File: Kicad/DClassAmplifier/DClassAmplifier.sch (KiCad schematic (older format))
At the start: 0 parts

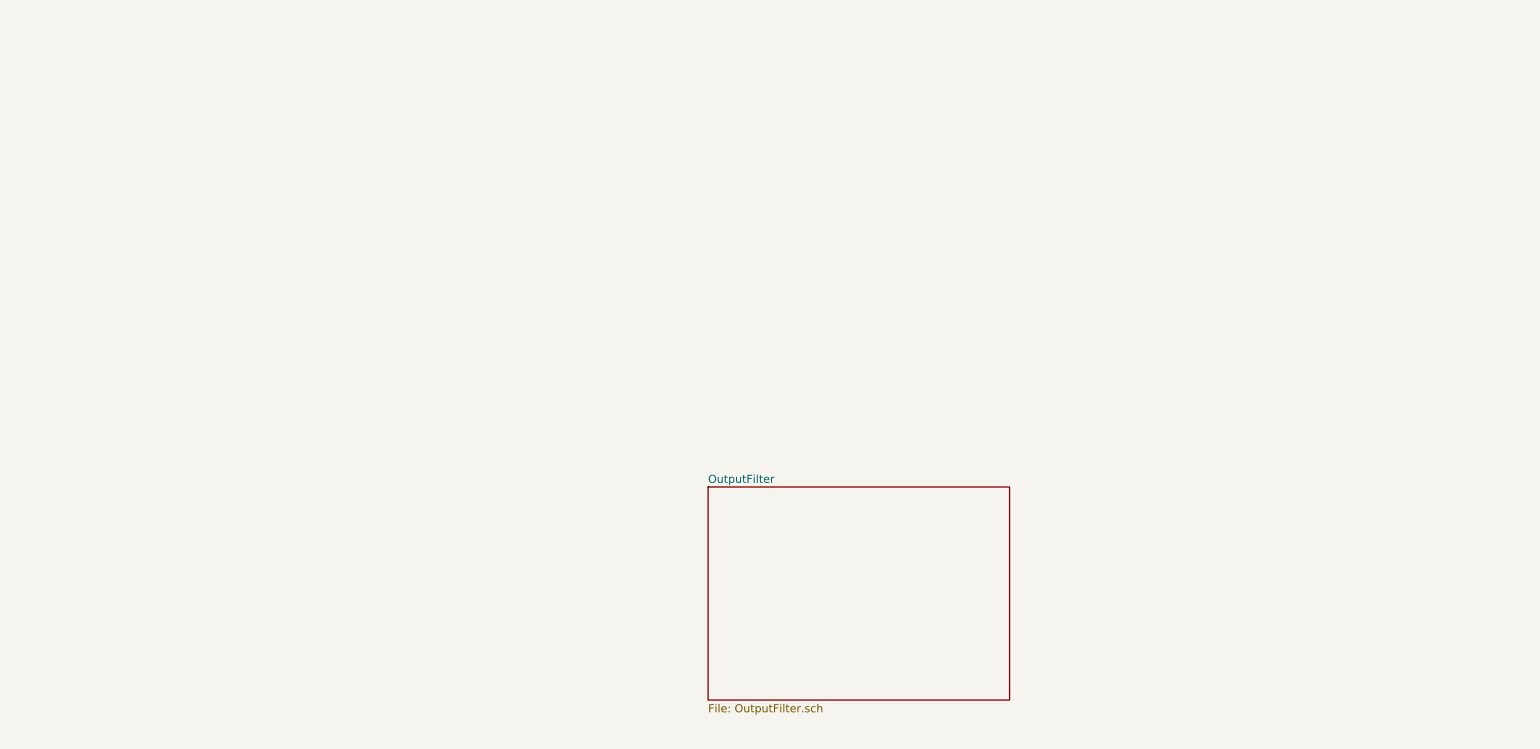
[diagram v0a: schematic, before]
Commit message: Added Net-Tied Grounds and Filter schematic
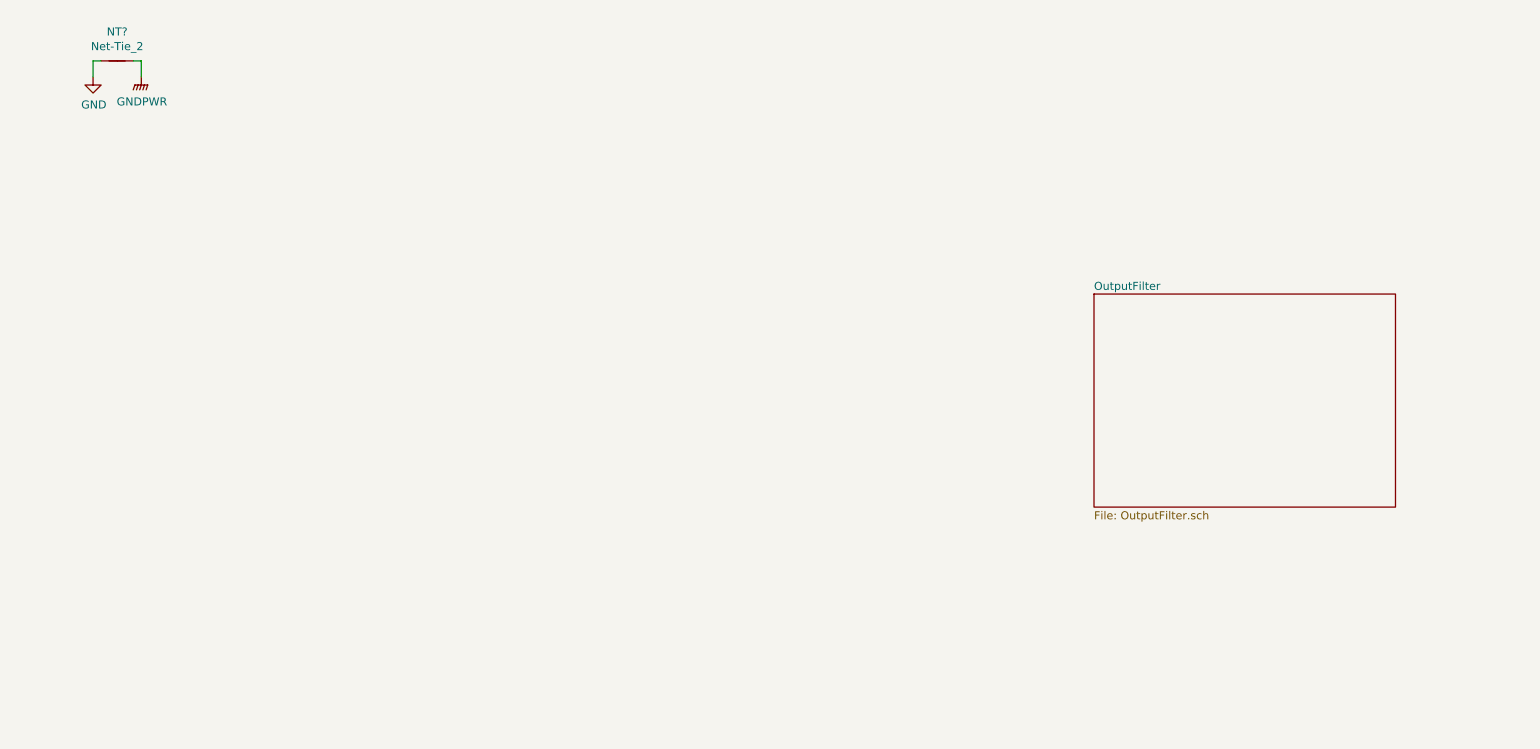
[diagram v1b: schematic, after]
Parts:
- added NT?: Net-Tie_2, NetTie:NetTie-2_SMD_Pad2.0mm, symbol Device:Net-Tie_2
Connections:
- new net GND: NT?.1
- new net GNDPWR: NT?.2
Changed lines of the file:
@@
 $EndDescr
 $Sheet
-S 4975 3550 1875 1325
+S 7375 2350 1875 1325
 U 60F78807
 F0 "OutputFilter" 50
 F1 "OutputFilter.sch" 50
 $EndSheet
+$Comp
+L power:GNDPWR #PWR?
+U 1 1 60FD17D7
+P 1450 1000
+F 0 "#PWR?" H 1450 800 50  0001 C CNN
+F 1 "GNDPWR" H 1454 846 50  0000 C CNN
+F 2 "" H 1450 950 50  0001 C CNN
+F 3 "" H 1450 950 50  0001 C CNN
+	1    1450 1000
+	1    0    0    -1
+$EndComp
+$Comp
+L power:GND #PWR?
+U 1 1 60FD1A94
+P 1150 1000
+F 0 "#PWR?" H 1150 750 50  0001 C CNN
+F 1 "GND" H 1155 827 50  0000 C CNN
+F 2 "" H 1150 1000 50  0001 C CNN
+F 3 "" H 1150 1000 50  0001 C CNN
+	1    1150 1000
+	1    0    0    -1
+$EndComp
+$Comp
+L Device:Net-Tie_2 NT?
+U 1 1 60FD21E0
+P 1300 900
+F 0 "NT?" H 1300 1081 50  0000 C CNN
+F 1 "Net-Tie_2" H 1300 990 50  0000 C CNN
+F 2 "NetTie:NetTie-2_SMD_Pad2.0mm" H 1300 900 50  0001 C CNN
+F 3 "~" H 1300 900 50  0001 C CNN
+	1    1300 900
+	1    0    0    -1
+$EndComp
+Wire Wire Line
+	1200 900  1150 900
+Wire Wire Line
+	1150 900  1150 1000
+Wire Wire Line
+	1400 900  1450 900
+Wire Wire Line
+	1450 900  1450 1000
 $EndSCHEMATC

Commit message: Create Additional Needed Hierarchical Schematics. Add Mounting Holes
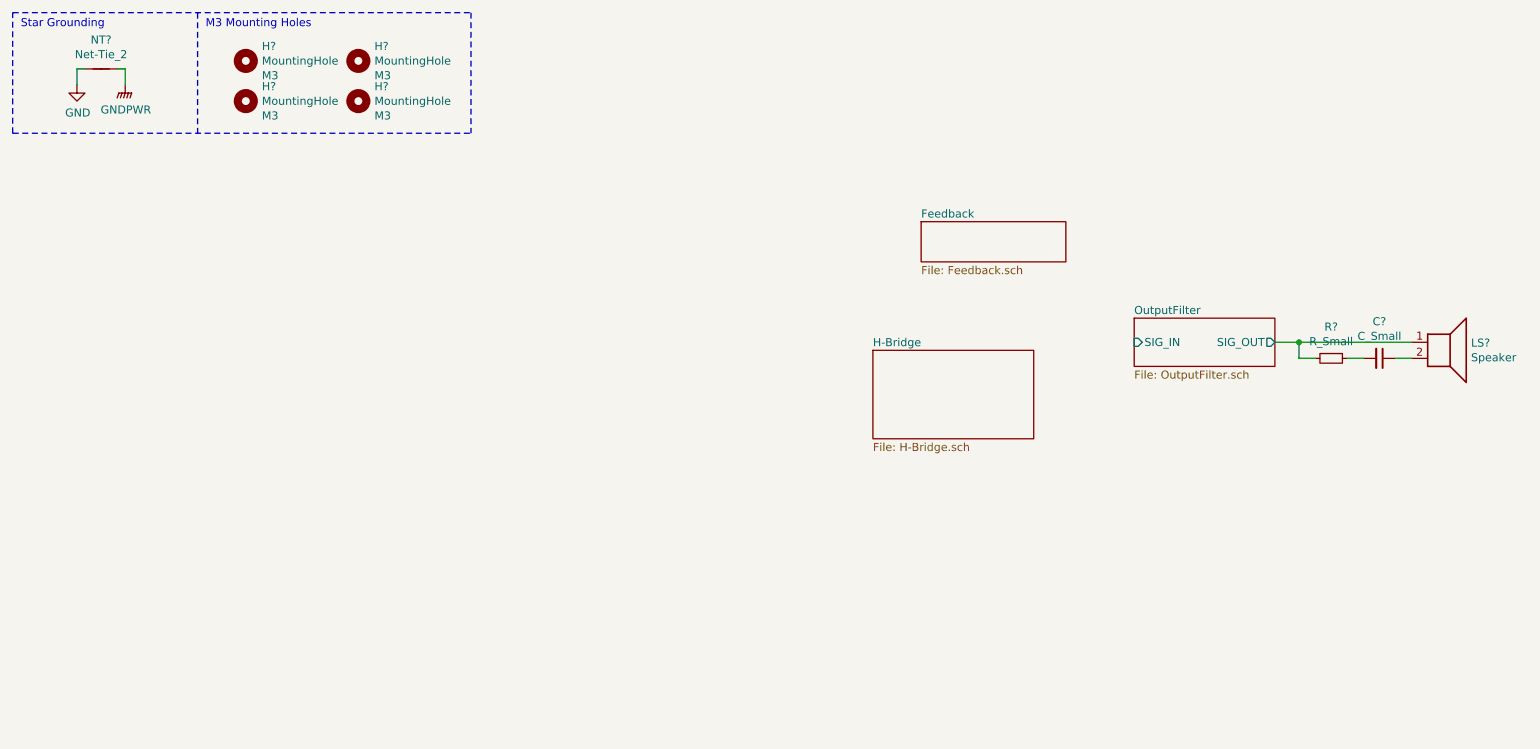
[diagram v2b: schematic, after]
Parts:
- added C?: C_Small, symbol Device:C_Small
- added H? (x4): MountingHole, MountingHole:MountingHole_3.2mm_M3_ISO7380_Pad, symbol Mechanical:MountingHole
- added LS?: Speaker, symbol Device:Speaker
- added R?: R_Small, symbol Device:R_Small
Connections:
- new net: C?.1, LS?.2
- new net: C?.2, R?.1
- new net OutputFilter/SIG_OUT: LS?.1, R?.2
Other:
- note added: "M3 Mounting Holes"
- note added: "Star Grounding"
- moved on the sheet: NT?
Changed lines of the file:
@@
 $Descr A4 11693 8268
 encoding utf-8
-Sheet 1 2
+Sheet 1 3
 Title ""
 Date ""
@@
 $EndDescr
 $Sheet
-S 7375 2350 1875 1325
+S 7625 2500 875  300
 U 60F78807
 F0 "OutputFilter" 50
 F1 "OutputFilter.sch" 50
+F2 "SIG_IN" I L 7625 2650 50
+F3 "SIG_OUT" O R 8500 2650 50
 $EndSheet
 $Comp
 L power:GNDPWR #PWR?
 U 1 1 60FD17D7
-P 1450 1000
-F 0 "#PWR?" H 1450 800 50  0001 C CNN
-F 1 "GNDPWR" H 1454 846 50  0000 C CNN
-F 2 "" H 1450 950 50  0001 C CNN
-F 3 "" H 1450 950 50  0001 C CNN
-	1    1450 1000
+P 1350 1050
+F 0 "#PWR?" H 1350 850 50  0001 C CNN
+F 1 "GNDPWR" H 1354 896 50  0000 C CNN
+F 2 "" H 1350 1000 50  0001 C CNN
+F 3 "" H 1350 1000 50  0001 C CNN
+	1    1350 1050
 	1    0    0    -1
 $EndComp
@@
 L power:GND #PWR?
 U 1 1 60FD1A94
-P 1150 1000
-F 0 "#PWR?" H 1150 750 50  0001 C CNN
-F 1 "GND" H 1155 827 50  0000 C CNN
-F 2 "" H 1150 1000 50  0001 C CNN
-F 3 "" H 1150 1000 50  0001 C CNN
-	1    1150 1000
+P 1050 1050
+F 0 "#PWR?" H 1050 800 50  0001 C CNN
+F 1 "GND" H 1055 877 50  0000 C CNN
+F 2 "" H 1050 1050 50  0001 C CNN
+F 3 "" H 1050 1050 50  0001 C CNN
+	1    1050 1050
 	1    0    0    -1
 $EndComp
@@
 L Device:Net-Tie_2 NT?
 U 1 1 60FD21E0
-P 1300 900
-F 0 "NT?" H 1300 1081 50  0000 C CNN
-F 1 "Net-Tie_2" H 1300 990 50  0000 C CNN
-F 2 "NetTie:NetTie-2_SMD_Pad2.0mm" H 1300 900 50  0001 C CNN
-F 3 "~" H 1300 900 50  0001 C CNN
-	1    1300 900
+P 1200 950
+F 0 "NT?" H 1200 1131 50  0000 C CNN
+F 1 "Net-Tie_2" H 1200 1040 50  0000 C CNN
+F 2 "NetTie:NetTie-2_SMD_Pad2.0mm" H 1200 950 50  0001 C CNN
+F 3 "~" H 1200 950 50  0001 C CNN
+	1    1200 950
 	1    0    0    -1
 $EndComp
 Wire Wire Line
-	1200 900  1150 900
+	1100 950  1050 950
 Wire Wire Line
-	1150 900  1150 1000
+	1050 950  1050 1050
 Wire Wire Line
-	1400 900  1450 900
+	1300 950  1350 950
 Wire Wire Line
-	1450 900  1450 1000
+	1350 950  1350 1050
+$Comp
+L Device:Speaker LS?
+U 1 1 60FD7EA0
+P 9550 2650
+F 0 "LS?" H 9720 2646 50  0000 L CNN
+F 1 "Speaker" H 9720 2555 50  0000 L CNN
+F 2 "" H 9550 2450 50  0001 C CNN
+F 3 "~" H 9540 2600 50  0001 C CNN
+	1    9550 2650
+	1    0    0    -1
+$EndComp
+Wire Wire Line
+	9350 2650 8650 2650
+$Comp
+L Device:R_Small R?
+U 1 1 60FD8CE8
+P 8850 2750
+F 0 "R?" V 8654 2750 50  0000 C CNN
+F 1 "R_Small" V 8745 2750 50  0000 C CNN
+F 2 "" H 8850 2750 50  0001 C CNN
+F 3 "~" H 8850 2750 50  0001 C CNN
+	1    8850 2750
+	0    1    1    0
+$EndComp
+$Comp
+L Device:C_Small C?
+U 1 1 60FD982C
+P 9150 2750
+F 0 "C?" V 8921 2750 50  0000 C CNN
+F 1 "C_Small" V 9012 2750 50  0000 C CNN
+F 2 "" H 9150 2750 50  0001 C CNN
+F 3 "~" H 9150 2750 50  0001 C CNN
+	1    9150 2750
+	0    1    1    0
+$EndComp
+Wire Wire Line
+	9250 2750 9350 2750
+Wire Wire Line
+	9050 2750 8950 2750
+Wire Wire Line
+	8750 2750 8650 2750
+Wire Wire Line
+	8650 2750 8650 2650
+Connection ~ 8650 2650
+Wire Wire Line
+	8650 2650 8500 2650
+$Sheet
+S 6300 1900 900  250
+U 60FDBAA4
+F0 "Feedback" 50
+F1 "Feedback.sch" 50
+$EndSheet
+$Sheet
+S 6000 2700 1000 550
+U 60FDBB90
+F0 "H-Bridge" 50
+F1 "H-Bridge.sch" 50
+$EndSheet
+$Comp
+L Mechanical:MountingHole H?
+U 1 1 60FDDA7B
+P 2100 900
+F 0 "H?" H 2200 991 50  0000 L CNN
+F 1 "MountingHole" H 2200 900 50  0000 L CNN
+F 2 "MountingHole:MountingHole_3.2mm_M3_ISO7380_Pad" H 2100 900 50  0001 C CNN
+F 3 "~" H 2100 900 50  0001 C CNN
+F 4 "Standard dictates Hex Socket Button Heads" H 2100 900 50  0001 C CNN "Notes"
+F 5 "M3" H 2200 809 50  0000 L CNN "ScrewSize"
+	1    2100 900
+	1    0    0    -1
+$EndComp
+$Comp
+L Mechanical:MountingHole H?
+U 1 1 60FDF5F8
+P 2100 1150
+F 0 "H?" H 2200 1241 50  0000 L CNN
+F 1 "MountingHole" H 2200 1150 50  0000 L CNN
+F 2 "MountingHole:MountingHole_3.2mm_M3_ISO7380_Pad" H 2100 1150 50  0001 C CNN
+F 3 "~" H 2100 1150 50  0001 C CNN
+F 4 "Standard dictates Hex Socket Button Heads" H 2100 1150 50  0001 C CNN "Notes"
+F 5 "M3" H 2200 1059 50  0000 L CNN "ScrewSize"
+	1    2100 1150
+	1    0    0    -1
+$EndComp
+$Comp
+L Mechanical:MountingHole H?
+U 1 1 60FDFD61
+P 2800 900
+F 0 "H?" H 2900 991 50  0000 L CNN
+F 1 "MountingHole" H 2900 900 50  0000 L CNN
+F 2 "MountingHole:MountingHole_3.2mm_M3_ISO7380_Pad" H 2800 900 50  0001 C CNN
+F 3 "~" H 2800 900 50  0001 C CNN
+F 4 "Standard dictates Hex Socket Button Heads" H 2800 900 50  0001 C CNN "Notes"
+F 5 "M3" H 2900 809 50  0000 L CNN "ScrewSize"
+	1    2800 900
+	1    0    0    -1
+$EndComp
+$Comp
+L Mechanical:MountingHole H?
+U 1 1 60FDFFD3
+P 2800 1150
+F 0 "H?" H 2900 1241 50  0000 L CNN
+F 1 "MountingHole" H 2900 1150 50  0000 L CNN
+F 2 "MountingHole:MountingHole_3.2mm_M3_ISO7380_Pad" H 2800 1150 50  0001 C CNN
+F 3 "~" H 2800 1150 50  0001 C CNN
+F 4 "Standard dictates Hex Socket Button Heads" H 2800 1150 50  0001 C CNN "Notes"
+F 5 "M3" H 2900 1059 50  0000 L CNN "ScrewSize"
+	1    2800 1150
+	1    0    0    -1
+$EndComp
+Wire Notes Line
+	1800 600  1800 1350
+Wire Notes Line
+	650  1350 650  600
+Wire Notes Line
+	3500 600  3500 1350
+Wire Notes Line
+	650  600  3500 600
+Wire Notes Line
+	650  1350 3500 1350
+Text Notes 700  700  0    50   ~ 0
+Star Grounding
+Text Notes 1850 700  0    50   ~ 0
+M3 Mounting Holes
 $EndSCHEMATC

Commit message: FET Selection
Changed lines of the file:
@@
 F0 "H-Bridge" 50
 F1 "H-Bridge.sch" 50
+F2 "PWM" I L 6000 2950 50
+F3 "V_OUT1" O R 7000 2950 50
 $EndSheet
 $Comp
@@
 Text Notes 1850 700  0    50   ~ 0
 M3 Mounting Holes
+Wire Wire Line
+	7625 2650 7475 2650
+Wire Wire Line
+	7475 2650 7475 2950
+Wire Wire Line
+	7475 2950 7000 2950
 $EndSCHEMATC

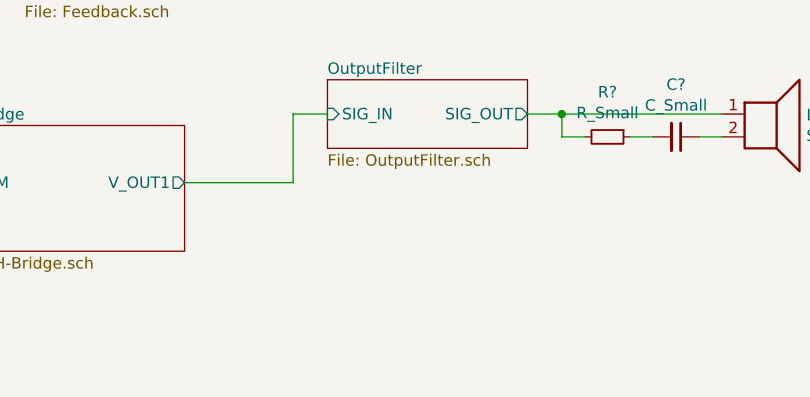
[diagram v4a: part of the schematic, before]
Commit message: Sizing Gate Driver Components
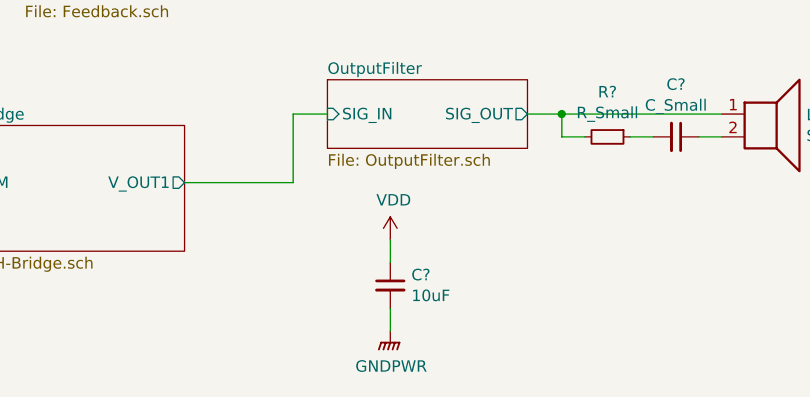
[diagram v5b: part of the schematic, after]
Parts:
- added C?: 10uF, symbol Device:C_Small
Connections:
- net GNDPWR: now also C?.2
- new net VDD: C?.1
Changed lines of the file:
@@
 Wire Wire Line
 	7475 2950 7000 2950
+$Comp
+L power:VDD #PWR?
+U 1 1 6101A943
+P 7900 3200
+F 0 "#PWR?" H 7900 3050 50  0001 C CNN
+F 1 "VDD" H 7915 3373 50  0000 C CNN
+F 2 "" H 7900 3200 50  0001 C CNN
+F 3 "" H 7900 3200 50  0001 C CNN
+	1    7900 3200
+	1    0    0    -1
+$EndComp
+$Comp
+L power:GNDPWR #PWR?
+U 1 1 6101A949
+P 7900 3600
+F 0 "#PWR?" H 7900 3400 50  0001 C CNN
+F 1 "GNDPWR" H 7904 3446 50  0000 C CNN
+F 2 "" H 7900 3550 50  0001 C CNN
+F 3 "" H 7900 3550 50  0001 C CNN
+	1    7900 3600
+	1    0    0    -1
+$EndComp
+$Comp
+L Device:C_Small C?
+U 1 1 6101A94F
+P 7900 3400
+AR Path="/60FDBB90/6101A94F" Ref="C?"  Part="1"
+AR Path="/6101A94F" Ref="C?"  Part="1"
+F 0 "C?" H 7992 3446 50  0000 L CNN
+F 1 "10uF" H 7992 3355 50  0000 L CNN
+F 2 "" H 7900 3400 50  0001 C CNN
+F 3 "~" H 7900 3400 50  0001 C CNN
+	1    7900 3400
+	1    0    0    -1
+$EndComp
+Wire Wire Line
+	7900 3600 7900 3500
+Wire Wire Line
+	7900 3200 7900 3300
 $EndSCHEMATC
